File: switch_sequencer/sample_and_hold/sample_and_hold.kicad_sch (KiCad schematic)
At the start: 38 parts, among them J12 Eurorack_Power_10pin_Shrouded, J14 3.5mm_Mono_Switched_sm, J15 3.5mm_Mono_Switched_sm, J16 3.5mm_Mono_Switched_sm, J17 3.5mm_Mono_Switched_sm, J18 3.5mm_Mono_Switched_sm, J19 3.5mm_Mono_Switched_sm, U1 TL072, U2 LF398_SOIC8, U3 TL072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

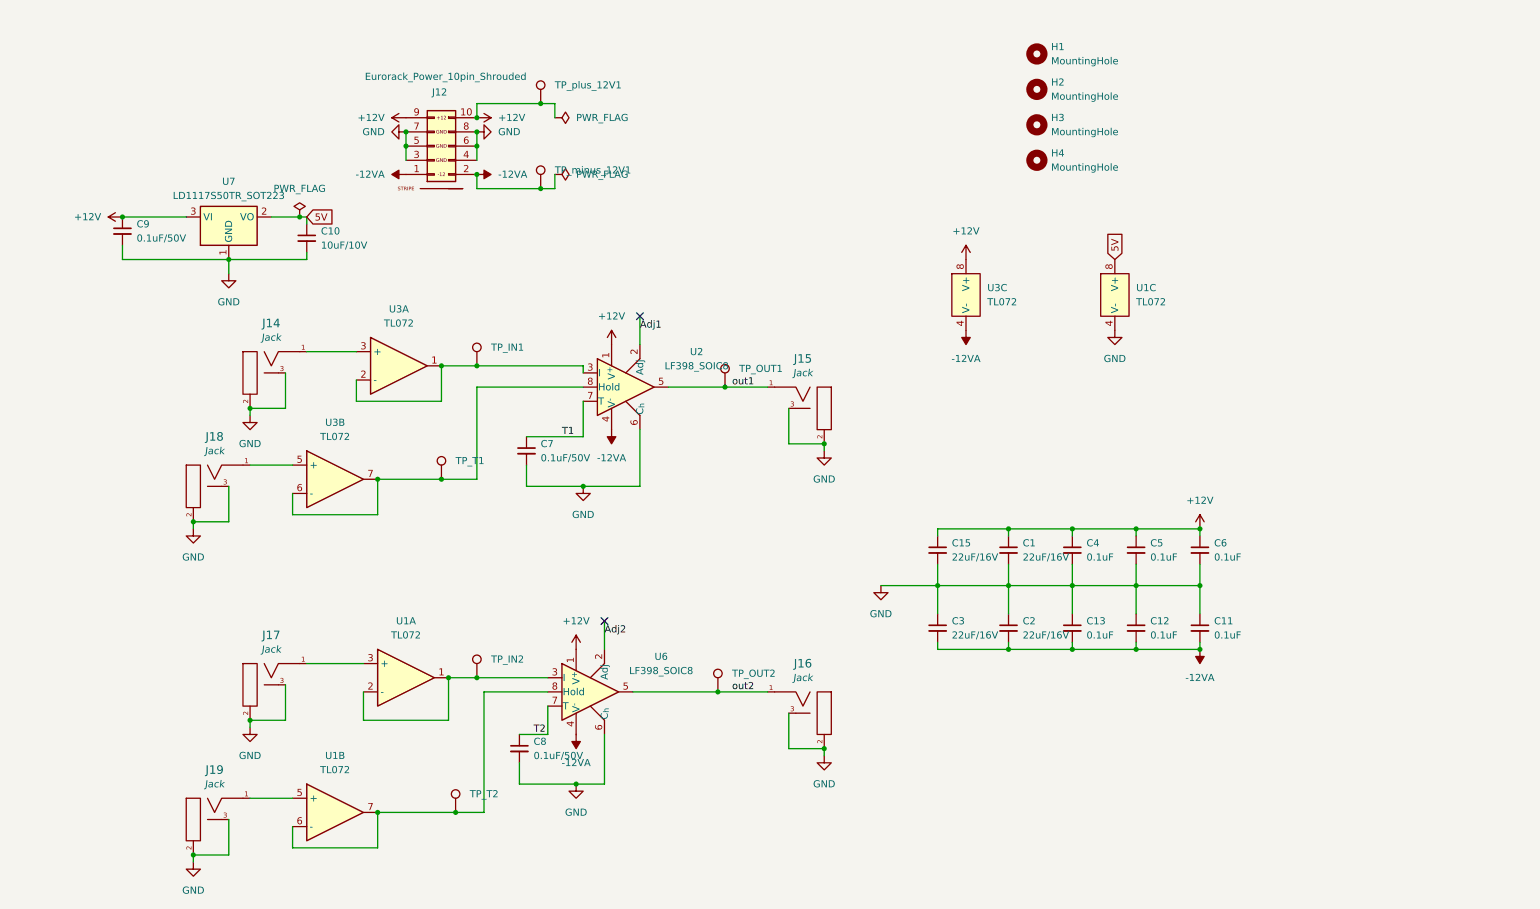
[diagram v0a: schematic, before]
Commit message: finish attenuverters, sample and hold
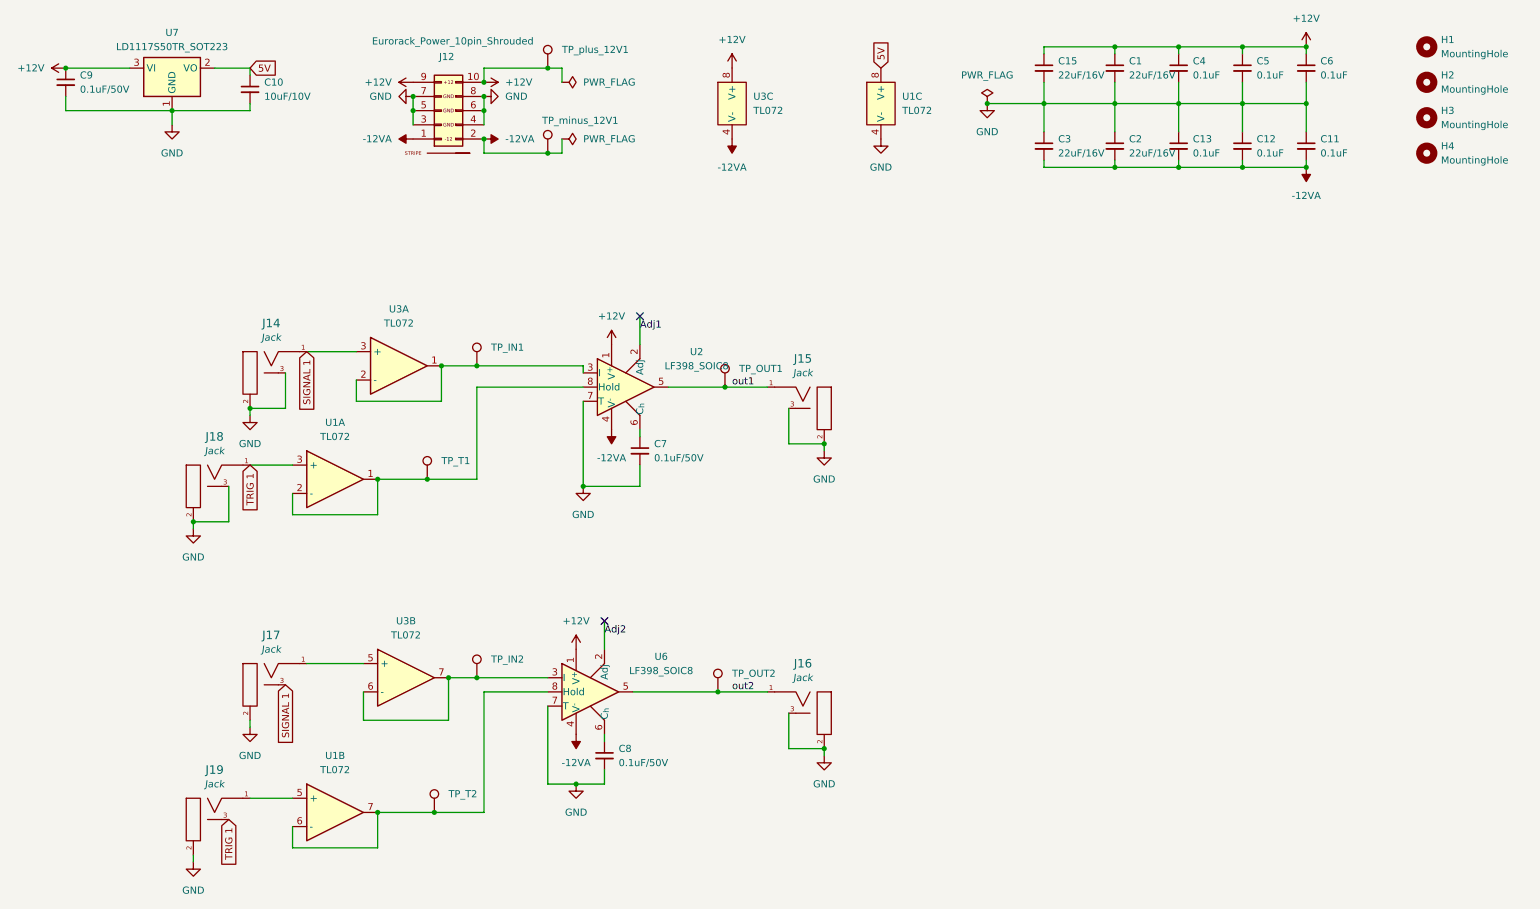
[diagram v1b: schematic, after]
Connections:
- net GND: now also U2.7 (T), U6.7 (T); no longer J17.3 (SW), J19.3 (SW), U2.6 (C_{h}), U6.6 (C_{h})
- net at U1.1, U1.2 (-): now also TP_T1.1, U2.8 (Hold); no longer TP_IN2.1, U6.3 (I)
- net at J17.1 (SIG): now also U3.5 (+); no longer U1.3 (+)
- net TRIG 1: now reaches J18.1 (SIG)
- net TRIG 1: now also J19.3 (SW), U1.3 (+); no longer U3.5 (+)
- net SIGNAL 1: now reaches J14.1 (SIG), U3.3 (+)
- net SIGNAL 1: now also J17.3 (SW)
- net at U3.6 (-), U3.7: now also TP_IN2.1, U6.3 (I); no longer TP_T1.1, U2.8 (Hold)
- net T1: no longer names the net of C7.1
- net T1: now also U2.6 (C_{h}); no longer U2.7 (T)
- net T2: no longer names the net of C8.1
- net T2: now also U6.6 (C_{h}); no longer U6.7 (T)
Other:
- moved on the sheet: C1, C10, C11, C12, C13, C15, C2, C3, C4, C5, C6, C9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
